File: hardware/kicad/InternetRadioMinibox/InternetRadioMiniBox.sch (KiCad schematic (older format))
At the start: 62 parts, among them IC1 ESP8266, IC2 ATMEGA328P-P, IC3 23K256, IC4 VS1011e, IC5 LM386, M1 TSR1-2433, M2 TSR1-2433, M3 TSR1-2433, P1 CONN_01X02, P2 CONN_01X02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

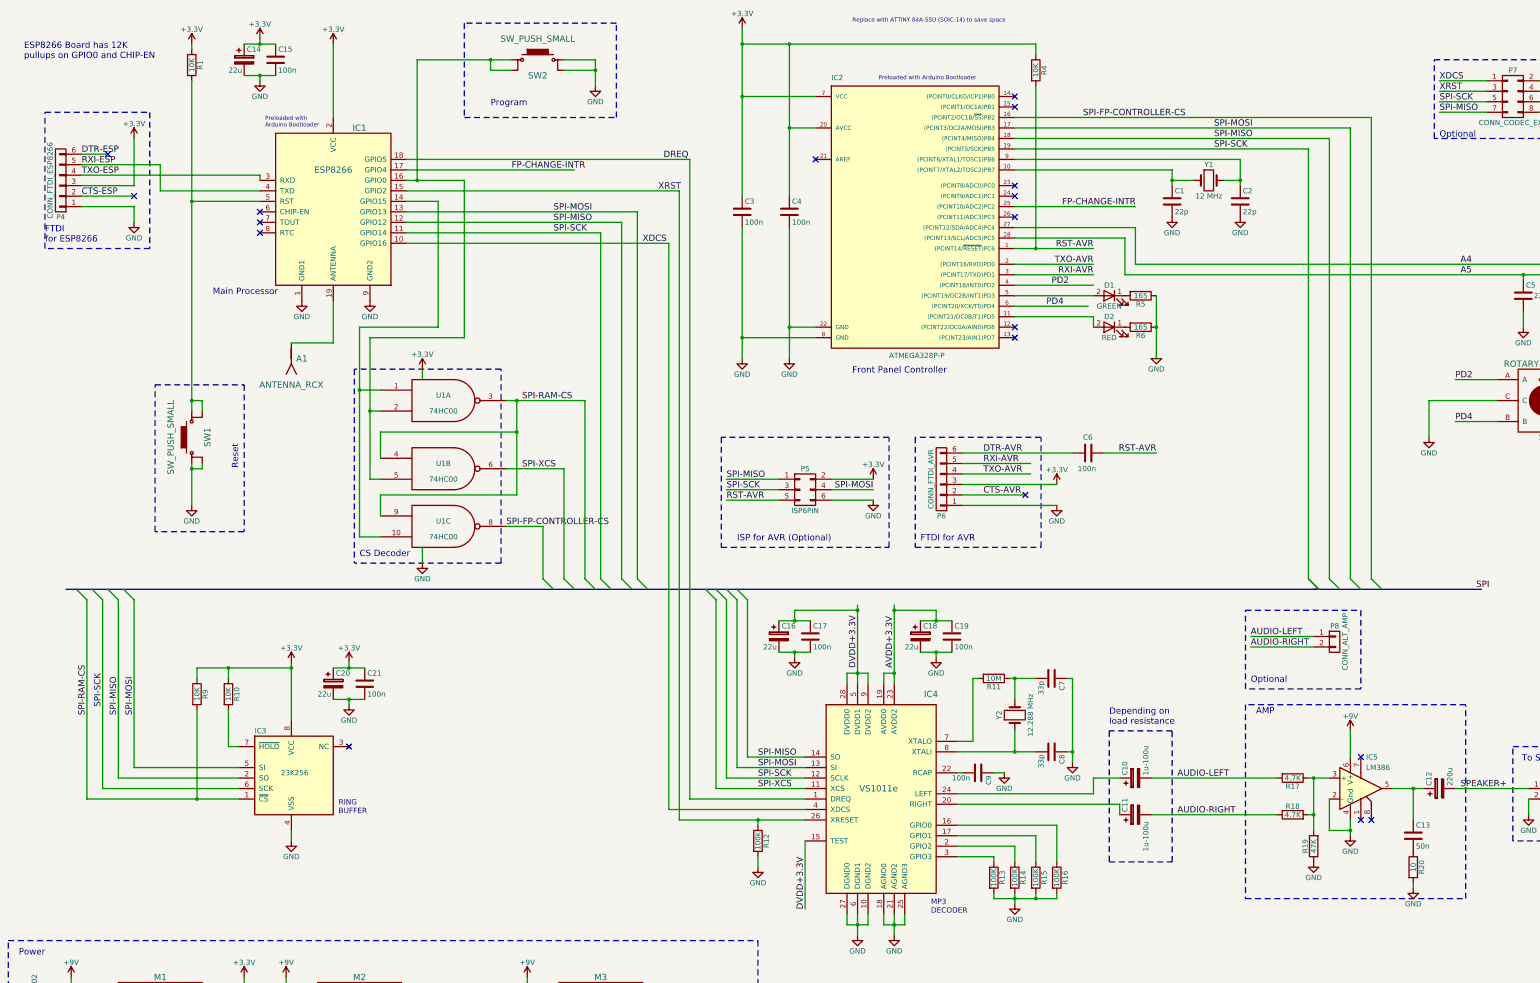
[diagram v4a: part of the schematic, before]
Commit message: Replaced ESP8266 with Adafruit Feather M0
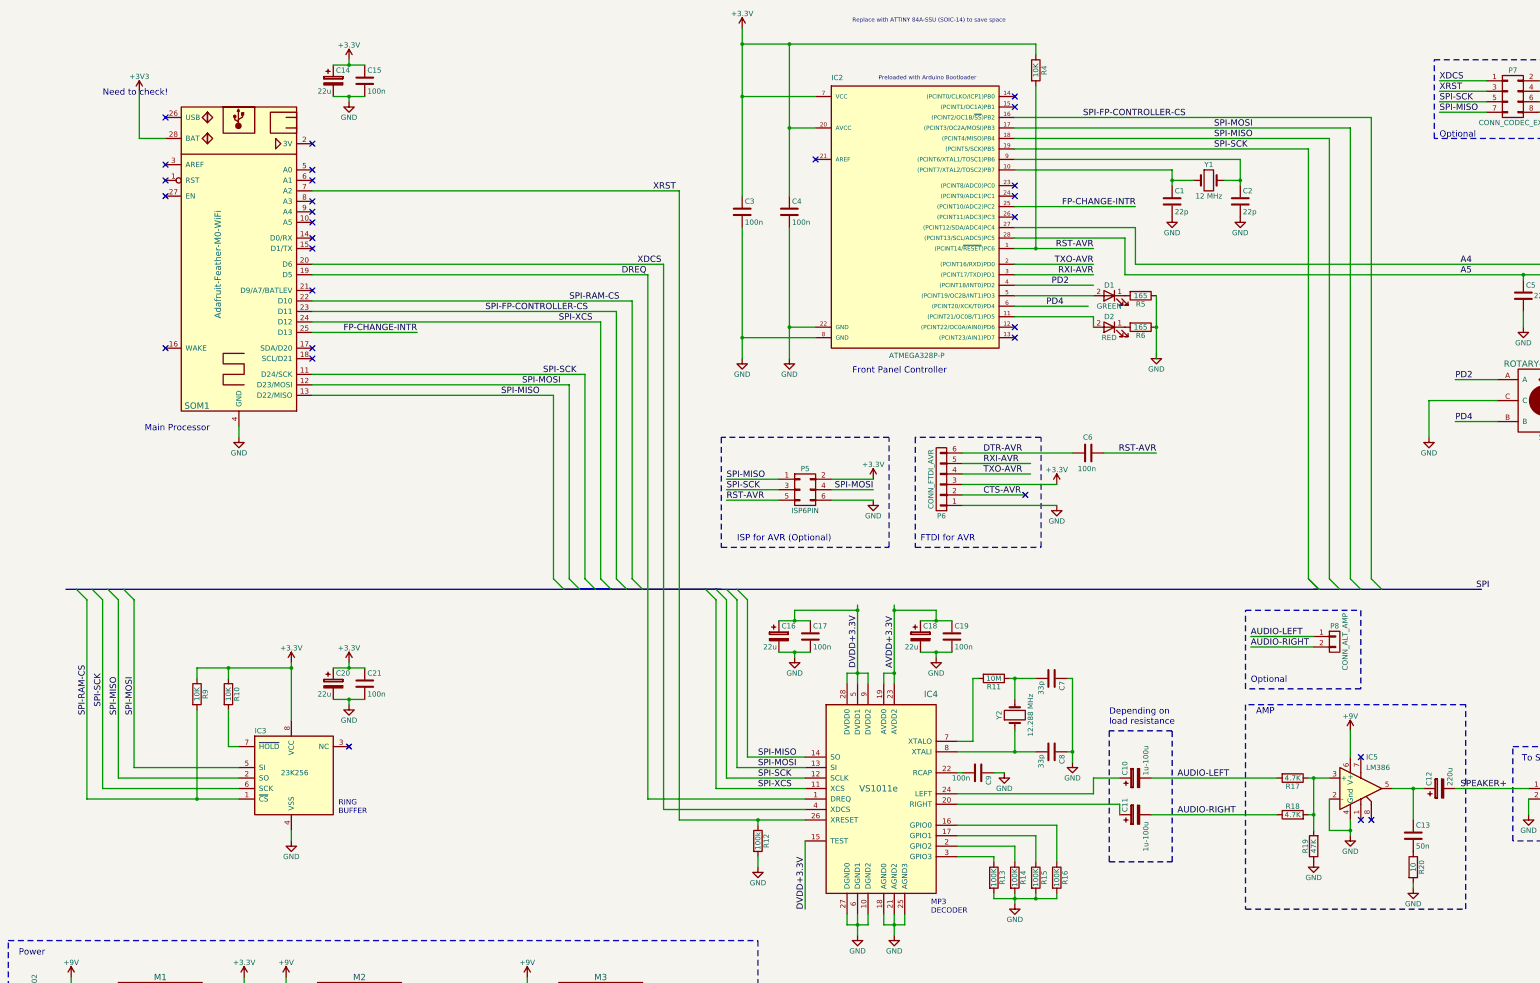
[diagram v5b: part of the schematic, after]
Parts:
- removed A1: ANTENNA_RCX, symbol ANTENNA_RCX
- removed IC1: ESP8266, maker:ESP8266-IN-CIRCUIT, symbol ESP8266
- removed P4: CONN_FTDI_ESP8266, Connect:PINHEAD1-6, symbol CONN_01X06
- removed R1: 10K, Resistors_SMD:R_0805_HandSoldering, symbol R
- removed SW1, SW2: SW_PUSH_SMALL, maker:SMALL_PUSH_BUTTON, symbol SW_PUSH_SMALL-RESCUE-InternetRadioMiniBox
- removed U1: 74HC00, symbol 74HC00
- added SOM1: Adafruit-Feather-M0-WiFi, symbol Adafruit-Feather-M0-WiFi
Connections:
- net labels added: +3V3
- net labels removed: CTS-ESP, DTR-ESP, RXI-ESP, TXO-ESP
- wire segments 317 -> 263
- no-connect marks 18 -> 29
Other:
- note added: "Need to check!"
- note removed: "CS Decoder\n"
- note removed: "ESP8266 Board has 12K \npullups on GPIO0 and CHIP-EN"
- note removed: "FTDI\nfor ESP8266"
- note removed: "Preloaded with \nArduino Bootloader"
- note removed: "Program"
- note removed: "Reset"
- moved on the sheet: C14, C15

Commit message: Changed wiring to use another SERCOM for the SPI bus
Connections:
- wire segments 263 -> 218
- no-connect marks 29 -> 28
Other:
- note added: "1"
- note added: "16"
- note added: "17"
- note added: "28"
- note added: "Need to check!\nCheck forum answers!"
- note added: "Pinouts Feather M0"
- note removed: "Need to check!"

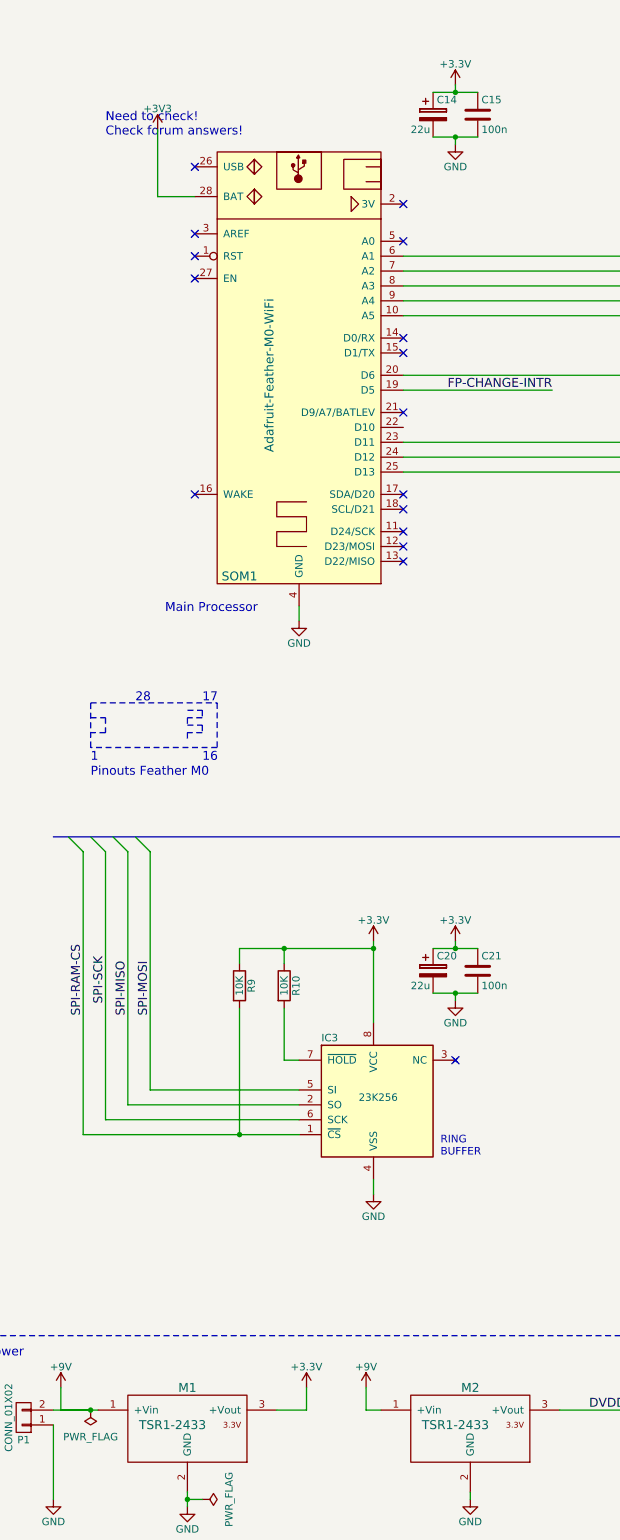
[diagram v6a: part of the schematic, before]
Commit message: New circuit using Adafruit Feather M0 WiFi
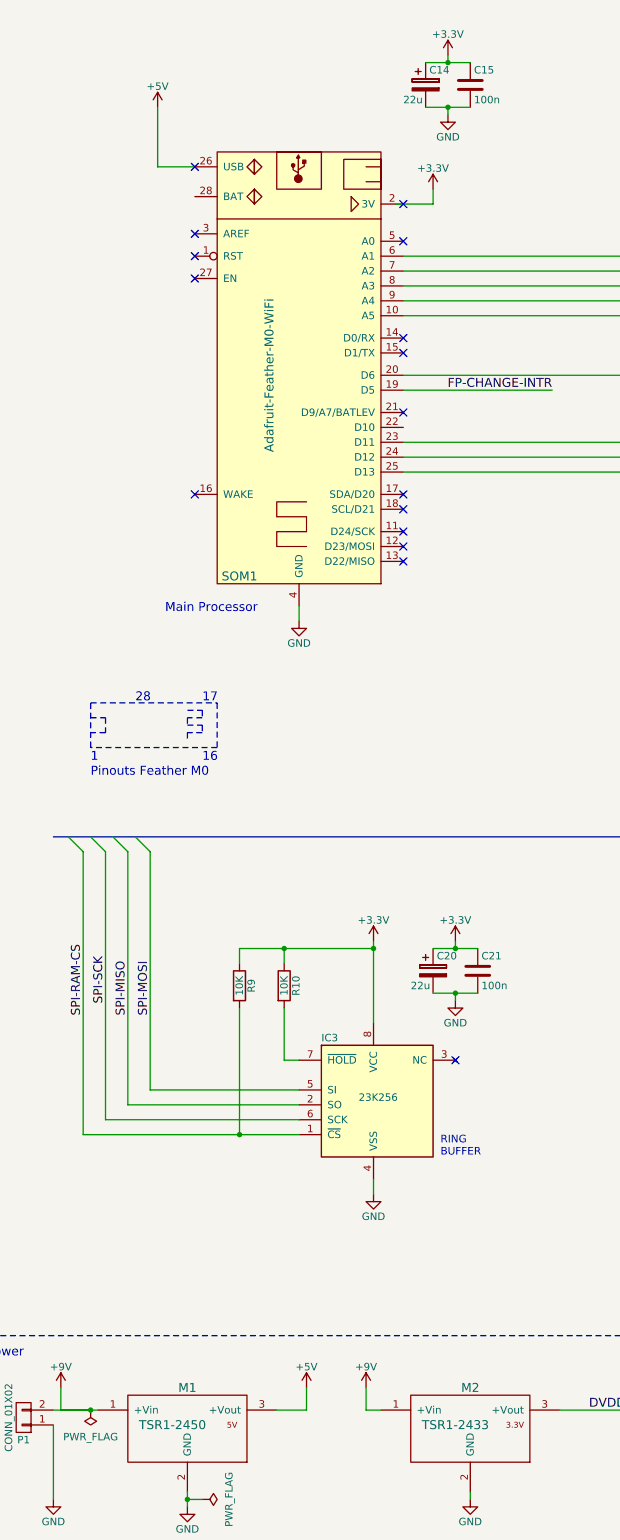
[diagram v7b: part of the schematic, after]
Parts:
- removed M1: TSR1-2433, maker:TSR1-2433, symbol TSR1-2433
- added M1: TSR1-2450, symbol TSR1-2450
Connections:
- net labels added: +5V
- net labels removed: +3V3
- wire segments 218 -> 220
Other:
- note removed: "Need to check!\nCheck forum answers!"
- moved on the sheet: C14, C15
